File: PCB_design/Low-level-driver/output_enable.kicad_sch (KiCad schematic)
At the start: 6 parts, among them Q501 Q_NPN_EBC, Q502 PMOS

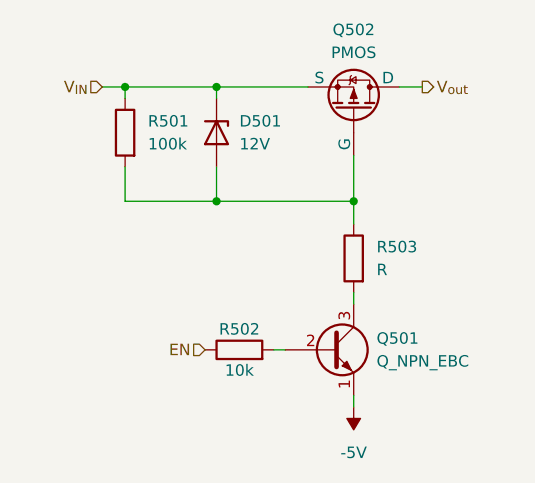
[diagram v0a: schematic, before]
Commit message: Schematic hierarchical redesign
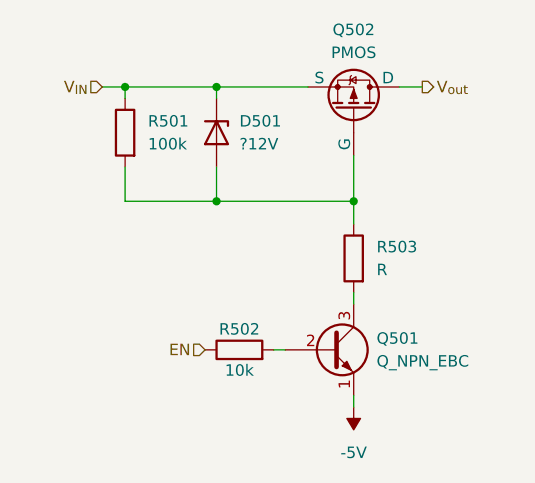
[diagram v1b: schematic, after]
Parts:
- D501: value 12V -> ?12V
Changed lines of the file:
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@@
 		(instances
 			(project "Low-level-driver"
-				(path "/2e43a8c9-1b23-4896-a481-133b23afb346/7d6c0230-91b3-4a2a-9a09-3f3403bcba97"
+				(path "/2e43a8c9-1b23-4896-a481-133b23afb346/016df87f-c803-44fb-9ff3-a33dc71d7c4c"
+					(reference "R603")
+					(unit 1)
+				)
+				(path "/2e43a8c9-1b23-4896-a481-133b23afb346/9363c3cd-da89-4013-abbb-a8f39df5ef51"
 					(reference "R503")
-					(unit 1)
-				)
-				(path "/2e43a8c9-1b23-4896-a481-133b23afb346/ef1af7e8-3f5a-4110-91c9-f8ee26645e73"
-					(reference "R403")
 					(unit 1)
 				)
@@
 		(instances
 			(project "Low-level-driver"
-				(path "/2e43a8c9-1b23-4896-a481-133b23afb346/7d6c0230-91b3-4a2a-9a09-3f3403bcba97"
+				(path "/2e43a8c9-1b23-4896-a481-133b23afb346/016df87f-c803-44fb-9ff3-a33dc71d7c4c"
+					(reference "Q602")
+					(unit 1)
+				)
+				(path "/2e43a8c9-1b23-4896-a481-133b23afb346/9363c3cd-da89-4013-abbb-a8f39df5ef51"
 					(reference "Q502")
-					(unit 1)
-				)
-				(path "/2e43a8c9-1b23-4896-a481-133b23afb346/ef1af7e8-3f5a-4110-91c9-f8ee26645e73"
-					(reference "Q402")
 					(unit 1)
 				)
@@
 		(instances
 			(project "Low-level-driver"
-				(path "/2e43a8c9-1b23-4896-a481-133b23afb346/7d6c0230-91b3-4a2a-9a09-3f3403bcba97"
+				(path "/2e43a8c9-1b23-4896-a481-133b23afb346/016df87f-c803-44fb-9ff3-a33dc71d7c4c"
+					(reference "R601")
+					(unit 1)
+				)
+				(path "/2e43a8c9-1b23-4896-a481-133b23afb346/9363c3cd-da89-4013-abbb-a8f39df5ef51"
 					(reference "R501")
-					(unit 1)
-				)
-				(path "/2e43a8c9-1b23-4896-a481-133b23afb346/ef1af7e8-3f5a-4110-91c9-f8ee26645e73"
-					(reference "R401")
 					(unit 1)
 				)
@@
 		(instances
 			(project "Low-level-driver"
-				(path "/2e43a8c9-1b23-4896-a481-133b23afb346/7d6c0230-91b3-4a2a-9a09-3f3403bcba97"
+				(path "/2e43a8c9-1b23-4896-a481-133b23afb346/016df87f-c803-44fb-9ff3-a33dc71d7c4c"
+					(reference "R602")
+					(unit 1)
+				)
+				(path "/2e43a8c9-1b23-4896-a481-133b23afb346/9363c3cd-da89-4013-abbb-a8f39df5ef51"
 					(reference "R502")
-					(unit 1)
-				)
-				(path "/2e43a8c9-1b23-4896-a481-133b23afb346/ef1af7e8-3f5a-4110-91c9-f8ee26645e73"
-					(reference "R402")
 					(unit 1)
 				)
@@
 		(instances
 			(project "Low-level-driver"
-				(path "/2e43a8c9-1b23-4896-a481-133b23afb346/7d6c0230-91b3-4a2a-9a09-3f3403bcba97"
+				(path "/2e43a8c9-1b23-4896-a481-133b23afb346/016df87f-c803-44fb-9ff3-a33dc71d7c4c"
+					(reference "Q601")
+					(unit 1)
+				)
+				(path "/2e43a8c9-1b23-4896-a481-133b23afb346/9363c3cd-da89-4013-abbb-a8f39df5ef51"
 					(reference "Q501")
-					(unit 1)
-				)
-				(path "/2e43a8c9-1b23-4896-a481-133b23afb346/ef1af7e8-3f5a-4110-91c9-f8ee26645e73"
-					(reference "Q401")
 					(unit 1)
 				)
@@
 		(instances
 			(project "Low-level-driver"
-				(path "/2e43a8c9-1b23-4896-a481-133b23afb346/7d6c0230-91b3-4a2a-9a09-3f3403bcba97"
+				(path "/2e43a8c9-1b23-4896-a481-133b23afb346/016df87f-c803-44fb-9ff3-a33dc71d7c4c"
+					(reference "#PWR0601")
+					(unit 1)
+				)
+				(path "/2e43a8c9-1b23-4896-a481-133b23afb346/9363c3cd-da89-4013-abbb-a8f39df5ef51"
 					(reference "#PWR0501")
-					(unit 1)
-				)
-				(path "/2e43a8c9-1b23-4896-a481-133b23afb346/ef1af7e8-3f5a-4110-91c9-f8ee26645e73"
-					(reference "#PWR0401")
 					(unit 1)
 				)
@@
 			)
 		)
-		(property "Value" "12V"
+		(property "Value" "?12V"
 			(at 69.85 72.3899 90)
 			(effects
@@
 		(instances
 			(project "Low-level-driver"
-				(path "/2e43a8c9-1b23-4896-a481-133b23afb346/7d6c0230-91b3-4a2a-9a09-3f3403bcba97"
+				(path "/2e43a8c9-1b23-4896-a481-133b23afb346/016df87f-c803-44fb-9ff3-a33dc71d7c4c"
+					(reference "D601")
+					(unit 1)
+				)
+				(path "/2e43a8c9-1b23-4896-a481-133b23afb346/9363c3cd-da89-4013-abbb-a8f39df5ef51"
 					(reference "D501")
 					(unit 1)
 				)
-				(path "/2e43a8c9-1b23-4896-a481-133b23afb346/ef1af7e8-3f5a-4110-91c9-f8ee26645e73"
-					(reference "D401")
-					(unit 1)
-				)
